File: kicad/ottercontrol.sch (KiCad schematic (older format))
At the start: 75 parts, among them IC1 MAX485, IC2 USBLC6-4, IC3 USBLC6-2SC6, J1 USB_B_Micro, P1 Conn_01x02, Q1 Q_PMOS_GSD, U1 STM32F303CBT6, U2 MAX3051, U6 XL7015, U7 ACT4088, U8 MIC5504-3.3YM5, X1 programmer, X2 Conn_01x08, X3 Conn_01x05, Y1 16MHz

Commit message: placed and routed; preliminary finished
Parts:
- added GND1, VDC1, VDC2: Conn_01x01, TestPoint:TestPoint_THTPad_4.0x4.0mm_Drill2.0mm, symbol Connector_Generic:Conn_01x01
- added R48: 0, Resistor_SMD:R_0603_1608Metric, symbol Device:R
- X1: footprint Connector_PinHeader_2.54mm:PinHeader_2x03_P2.54mm_Vertical -> Connector:Tag-Connect_TC2030-IDC-NL_2x03_P1.27mm_Vertical
- X2: footprint Connector_JST:JST_GH_SM08B-GHS-TB_1x08-1MP_P1.25mm_Horizontal -> Connector_Molex:Molex_PicoBlade_53261-0871_1x08-1MP_P1.25mm_Horizontal
- X3: footprint Connector_JST:JST_GH_SM05B-GHS-TB_1x05-1MP_P1.25mm_Horizontal -> Connector_Molex:Molex_PicoBlade_53261-0571_1x05-1MP_P1.25mm_Horizontal
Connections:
- net RS458_TX is gone; now on net RS485_TX: IC1.4 (DI), U1.21 (PB10)
- net +3V3: now also C5.1, U2.3 (VDD); no longer IC2.5 (VBUS), X3.5 (Pin_5)
- net +5V: now also IC2.5 (VBUS), X3.5 (Pin_5); no longer C5.1, U2.3 (VDD)
- net +VDC: now also VDC1.1 (Pin_1), VDC2.1 (Pin_1)
- net GND: now also R48.2
- net GNDPWR: now also GND1.1 (Pin_1), R48.1
- net at IC3.1 (IO1), J1.2 (D-): now also IC3.6 (IO1), R11.1
- net at IC3.3 (IO2), J1.3 (D+): now also IC3.4 (IO2), R12.2, R14.2
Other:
- moved on the sheet: C24, C25, C26, C27, C28, R11

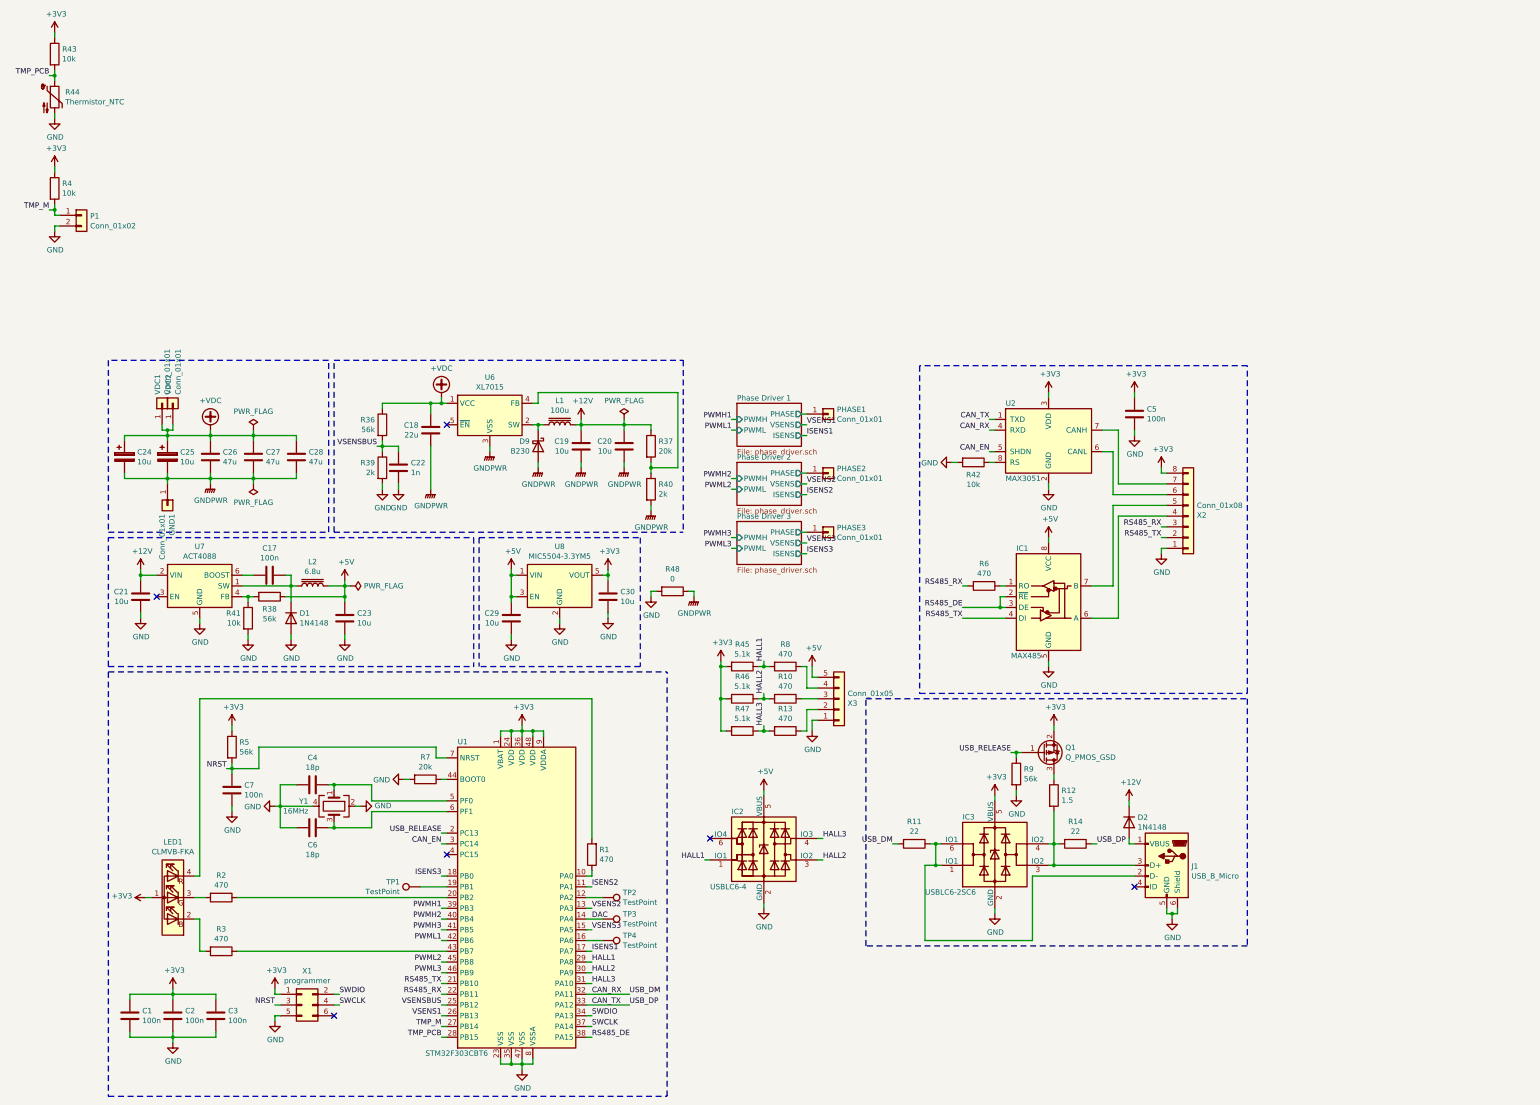
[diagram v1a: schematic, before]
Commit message: made footprint fot mosfets hybrid for TO220 and D2PAK; added jumper instead of 0 Ohm resistor
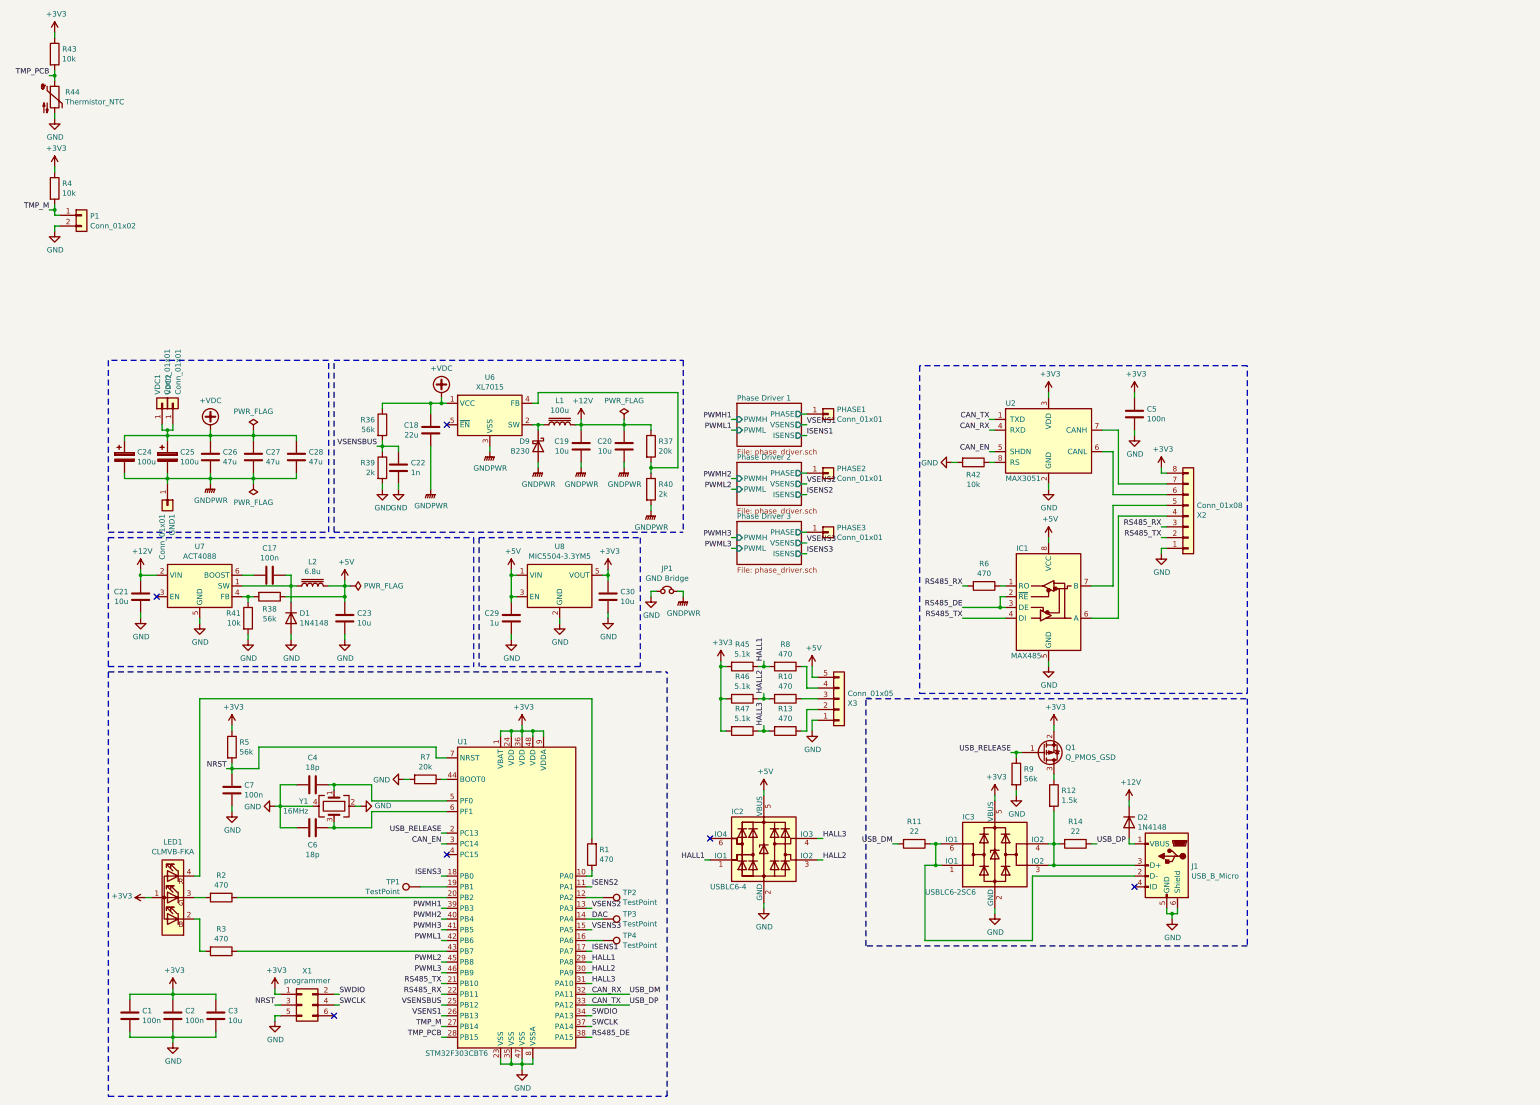
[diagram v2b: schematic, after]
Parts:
- removed R48: 0, Resistor_SMD:R_0603_1608Metric, symbol Device:R
- added JP1: GND Bridge, Jumper:SolderJumper-2_P1.3mm_Bridged_Pad1.0x1.5mm, symbol Device:Jumper_NC_Small
- C1, C2, C5, C7: MPN (none) -> GRM033C81E104KE14E; Voltage Rating DC (none) -> 25
- C17: MPN (none) -> CC0603MRY5V9BB104; Voltage Rating DC (none) -> 50
- C18: MPN (none) -> C5750X7R1E226M250KA; Voltage Rating DC (none) -> 100
- C19, C20, C21: MPN (none) -> TMK316BJ106KL-T; Voltage Rating DC (none) -> 25
- C22: MPN (none) -> 885012206083; Voltage Rating DC (none) -> 50
- C23, C30: MPN (none) -> JMK107ABJ106MA-T; Voltage Rating DC (none) -> 6.3
- C24, C25: value 10u -> 100u; MPN (none) -> 107CKS100MLQ; Voltage Rating DC (none) -> 100
- C26, C27, C28: MPN (none) -> CGA9N3X7R1E476M230KB; Voltage Rating DC (none) -> 100
- C29: value 10u -> 1u; MPN (none) -> 885012106022; Voltage Rating DC (none) -> 10
- C3: value 100n -> 10u; MPN (none) -> JMK107ABJ106MA-T; Voltage Rating DC (none) -> 6.3
- C4, C6: Dielectric (none) -> C0G (NP0); MPN (none) -> GRM0335C1E180FA01D; Tolerance (none) -> 1%
- D1, D2: MPN (none) -> 1N4148WS
- D9: MPN (none) -> B230AE-13
- IC1: MPN (none) -> MAX485CSA+
- IC2: MPN (none) -> USBLC6-4SC6
- IC3: MPN (none) -> USBLC6-2SC6
- L1: MPN (none) -> LPS6235-104MRC
- L2: MPN (none) -> LPS6235-682MRC
- LED1: MPN (none) -> ASMB-MTB0-0A3A2
- R1, R10, R13, R2, R3, R6, R8: MPN (none) -> RC0603FR-07470RL
- R11, R14: MPN (none) -> RC0603FR-0722RL
- R12: value 1.5 -> 1.5k; MPN (none) -> RC0603FR-071K5L
- R36, R38, R5, R9: MPN (none) -> RC0603FR-0756KL
- R37, R7: MPN (none) -> RC0603FR-0720KL
- R39, R40: MPN (none) -> RC0603FR-072KL
- R4, R41, R42, R43: MPN (none) -> RC0603FR-0710KL
- R45, R46, R47: MPN (none) -> RC0603FR-075K1L
- U1: MPN (none) -> STM32F303CBT6
- U2: MPN (none) -> MAX3051ESA+
- U7: MPN (none) -> ACT4088US-T
- U8: MPN (none) -> MIC5504-3.3YM5-TR
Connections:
- net GND: now also JP1.1
- net GNDPWR: now also JP1.2

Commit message: added finished adding MPNs to all components
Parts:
- C29: Voltage Rating DC 10 -> 25
- J1: MPN (none) -> 105017-0001
- JP1, TP1, TP2, TP3, TP4: MPN (none) -> n/a
- P1: renamed from X1; MPN (none) -> TC2030-MCP-NL
- P2: renamed from X2; MPN (none) -> 53261-0871
- P3: renamed from X3; MPN (none) -> 53261-0571
- P4: renamed from P1; MPN (none) -> n/a
- PAD1: renamed from PHASE1; MPN (none) -> n/a
- PAD2: renamed from PHASE2; MPN (none) -> n/a
- PAD3: renamed from PHASE3; MPN (none) -> n/a
- PAD4: renamed from VDC1; MPN (none) -> n/a
- PAD5: renamed from VDC2; MPN (none) -> n/a
- PAD6: renamed from GND1; MPN (none) -> n/a
- Q1: value Q_PMOS_GSD -> Si2367DS; MPN (none) -> SI2367DS-T1-GE3
- R1, R10, R13, R2, R3, R6, R8: MPN RC0603FR-07470RL -> RC0603FR-07100RL
- Y1: footprint Crystal:Crystal_SMD_5032-4Pin_5.0x3.2mm -> Crystal:Crystal_SMD_3225-4Pin_3.2x2.5mm; MPN (none) -> FA-238 16.0000MB-K3
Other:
- moved on the sheet: C29, C30, C5, D2, IC1, IC2, IC3, J1, JP1, P2, P3, P4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

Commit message: finalyzed design
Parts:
- removed IC3: USBLC6-2SC6, Package_TO_SOT_SMD:SOT-23-6, symbol Power_Protection:USBLC6-2SC6
- removed LED1: CLMVB-FKA, LED_SMD:LED_Cree-PLCC4_2x2mm_CW, symbol LED:ASMB-MTB0-0A3A2
- added IC3: USBLC6-4, Package_TO_SOT_SMD:SOT-23-6, symbol Power_Protection:USBLC6-4
- added LED1: LED_RABG, LED_SMD:LED_Avago_PLCC4_3.2x2.8mm_CW, symbol Device:LED_RABG
- C19, C20, C21: Aliexpress (none) -> https://www.aliexpress.com/item//32880416347.html
- C24, C25: Aliexpress (none) -> https://www.aliexpress.com/item//32642894401.html
- C26, C27, C28: Aliexpress (none) -> https://www.aliexpress.com/item//32826554052.html
- D9: Aliexpress (none) -> https://www.aliexpress.com/item//32855500127.html
- IC1: Aliexpress (none) -> https://de.aliexpress.com/item//32876836472.html
- IC2: Aliexpress (none) -> https://www.aliexpress.com/item//32917098748.html
- J1: Aliexpress (none) -> https://www.aliexpress.com/item//32857135081.html
- L1, L2: Aliexpress (none) -> https://de.aliexpress.com/item//32886534770.html
- P2: Aliexpress (none) -> https://de.aliexpress.com/item//32799039952.html
- P3: Aliexpress (none) -> https://de.aliexpress.com/item//32798651089.html
- Q1: Aliexpress (none) -> https://de.aliexpress.com/item//32964492474.html
- U1: Aliexpress (none) -> https://www.aliexpress.com/item//32745913400.html
- U2: Aliexpress (none) -> https://www.aliexpress.com/item//32915140112.html
- U6: Aliexpress (none) -> https://de.aliexpress.com/item//32955190374.html; MPN (none) -> XL7015
- U7: Aliexpress (none) -> https://de.aliexpress.com/item//32251221271.html
- U8: Aliexpress (none) -> https://de.aliexpress.com/item//32271737578.html
- Y1: Aliexpress (none) -> https://www.aliexpress.com/item//32851252873.html
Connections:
- net +3V3: now also IC3.5 (VBUS), LED1.2 (A)
- net GND: now also IC3.2 (GND)
- net at J1.2 (D-), R11.1: now also IC3.1 (IO1), IC3.6 (IO4)
- net at J1.3 (D+), R12.2, R14.2: now also IC3.3 (IO2), IC3.4 (IO3)
- net at R3.2: now also LED1.3 (BK)
- net at R2.2: now also LED1.4 (GK)
- net at R1.2: now also LED1.1 (RK)
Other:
- note added: "Cable Connector: 51021-0500\nhttps://de.aliexpress.com/item//32819174211.html"
- note added: "Cable Connector: 51021-0800\nhttps://de.aliexpress.com/item//32310864974.html"
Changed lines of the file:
@@
 encoding utf-8
 Sheet 1 4
-Title ""
-Date ""
+Title "ottercontrol"
+Date "2019-01-07"
 Rev ""
 Comp ""
@@
 F 3 "https://www.mouser.de/datasheet/2/389/stm32f303cb-956188.pdf" H 4350 5500 50  0001 C CNN
 F 4 "STM32F303CBT6" H 0   0   50  0001 C CNN "MPN"
+F 5 "https://www.aliexpress.com/item//32745913400.html" H 4350 5500 50  0001 C CNN "Aliexpress"
 	1    4350 5500
 	1    0    0    -1
@@
 F 3 "https://www.mouser.de/datasheet/2/137/A-238_en-932914.pdf" H 2600 4650 50  0001 C CNN
 F 4 "FA-238 16.0000MB-K3" H 0   0   50  0001 C CNN "MPN"
+F 5 "https://www.aliexpress.com/item//32851252873.html" V 2600 4650 50  0001 C CNN "Aliexpress"
 	1    2600 4650
 	0    1    1    0
@@
 F 3 "https://www.mouser.de/datasheet/2/256/MAX3051-1280983.pdf" H 9300 3550 50  0001 C CNN
 F 4 "MAX3051ESA+" H 50  2300 50  0001 C CNN "MPN"
+F 5 "https://www.aliexpress.com/item//32915140112.html" H 9300 3550 50  0001 C CNN "Aliexpress"
 	1    9300 3550
 	1    0    0    -1
@@
 F 3 "https://www.mouser.de/datasheet/2/256/MAX490-1389177.pdf" H 9300 5050 50  0001 C CNN
 F 4 "MAX485CSA+" H 50  2300 50  0001 C CNN "MPN"
+F 5 "https://de.aliexpress.com/item//32876836472.html" H 9300 5000 50  0001 C CNN "Aliexpress"
 	1    9300 5000
 	1    0    0    -1
@@
 F 3 "https://www.mouser.de/datasheet/2/276/0532610871_PCB_HEADERS-171054.pdf" H 10600 4250 50  0001 C CNN
 F 4 "53261-0871" H 50  2300 50  0001 C CNN "MPN"
+F 5 "https://de.aliexpress.com/item//32799039952.html" H 10600 4250 50  0001 C CNN "Aliexpress"
 	1    10600 4250
 	1    0    0    1
@@
 F 3 "https://www.mouser.de/datasheet/2/276/1050170001_IO_CONNECTORS-230168.pdf" H 10550 2000 50  0001 C CNN
 F 4 "105017-0001" H 50  -3150 50  0001 C CNN "MPN"
+F 5 "https://www.aliexpress.com/item//32857135081.html" H 10400 2050 50  0001 C CNN "Aliexpress"
 	1    10400 2050
 	-1   0    0    -1
@@
 F 3 "" H 8800 2500 50  0001 C CNN
 	1    8800 2500
-	1    0    0    -1
-$EndComp
-$Comp
-L Power_Protection:USBLC6-2SC6 IC3
-U 1 1 5C2EDA2E
-P 8800 1950
-F 0 "IC3" H 8500 2300 50  0000 L CNN
-F 1 "USBLC6-2SC6" H 8150 1600 50  0000 L CNN
-F 2 "Package_TO_SOT_SMD:SOT-23-6" H 8050 2350 50  0001 C CNN
-F 3 "https://www.mouser.de/datasheet/2/389/usblc6-2-957370.pdf" H 9000 2300 50  0001 C CNN
-F 4 "USBLC6-2SC6" H 50  -3150 50  0001 C CNN "MPN"
-	1    8800 1950
 	1    0    0    -1
 $EndComp
@@
 F 3 "https://www.mouser.de/datasheet/2/427/si2367ds-278436.pdf" H 9250 1000 50  0001 C CNN
 F 4 "SI2367DS-T1-GE3" H 50  -3150 50  0001 C CNN "MPN"
+F 5 "https://de.aliexpress.com/item//32964492474.html" H 9250 1000 50  0001 C CNN "Aliexpress"
 	1    9250 1000
 	1    0    0    1
@@
 $EndComp
 $Comp
-L LED:ASMB-MTB0-0A3A2 LED1
-U 1 1 5C47CE93
-P 1100 5500
-F 0 "LED1" H 1100 6017 50  0000 C CNN
-F 1 "CLMVB-FKA" H 1100 5926 50  0000 C CNN
-F 2 "LED_SMD:LED_Cree-PLCC4_2x2mm_CW" H 1100 6000 50  0001 C CNN
-F 3 "https://www.mouser.de/datasheet/2/678/V02-4186EN_DS_ASMB-MTB0_2014-09-10-909697.pdf" H 1100 5050 50  0001 C CNN
-F 4 "ASMB-MTB0-0A3A2" H 0   0   50  0001 C CNN "MPN"
-	1    1100 5500
-	-1   0    0    -1
-$EndComp
-$Comp
 L Regulator_Switching:APE1707H-12-HF U6
 U 1 1 5C58F2E9
@@
 F 2 "Package_TO_SOT_SMD:TO-252-5_TabPin3" H 4075 750 50  0001 L CIN
 F 3 "http://pdf.datasheet.live/datasheets-1/advanced_power_electronics/APE1707H-12-HF.pdf" H 4050 1000 50  0001 C CNN
-F 4 "" H 0   0   50  0001 C CNN "MPN"
+F 4 "XL7015" H 4150 1442 50  0001 C CNN "MPN"
+F 5 "https://de.aliexpress.com/item//32955190374.html" H 4050 1000 50  0001 C CNN "Aliexpress"
 	1    4050 1000
 	1    0    0    -1
@@
 F 3 "https://www.mouser.de/datasheet/2/115/B220AEBE-B245AEBE-1115122.pdf" H 4500 1300 50  0001 C CNN
 F 4 "B230AE-13" H 0   0   50  0001 C CNN "MPN"
+F 5 "https://www.aliexpress.com/item//32855500127.html" V 4500 1300 50  0001 C CNN "Aliexpress"
 	1    4500 1300
 	0    1    1    0
@@
 F 4 "25" H 4900 1300 50  0001 C CNN "Voltage Rating DC"
 F 5 "TMK316BJ106KL-T" H 0   0   50  0001 C CNN "MPN"
+F 6 "https://www.aliexpress.com/item//32880416347.html" H 4900 1300 50  0001 C CNN "Aliexpress"
 	1    4900 1300
 	1    0    0    -1
@@
 F 4 "25" H 5300 1300 50  0001 C CNN "Voltage Rating DC"
 F 5 "TMK316BJ106KL-T" H 0   0   50  0001 C CNN "MPN"
+F 6 "https://www.aliexpress.com/item//32880416347.html" H 5300 1300 50  0001 C CNN "Aliexpress"
 	1    5300 1300
 	1    0    0    -1
@@
 F 3 "https://www.mouser.de/datasheet/2/631/ACT4088_Datasheet-1291541.pdf" H 1250 2700 50  0001 C CNN
 F 4 "ACT4088US-T" H 0   0   50  0001 C CNN "MPN"
+F 5 "https://de.aliexpress.com/item//32251221271.html" H 1350 2600 50  0001 C CNN "Aliexpress"
 	1    1350 2600
 	1    0    0    -1
@@
 F 4 "25" H 800 2700 50  0001 C CNN "Voltage Rating DC"
 F 5 "TMK316BJ106KL-T" H 0   0   50  0001 C CNN "MPN"
+F 6 "https://www.aliexpress.com/item//32880416347.html" H 800 2700 50  0001 C CNN "Aliexpress"
 	1    800  2700
 	1    0    0    -1
@@
 F 3 "https://www.mouser.de/datasheet/2/597/lps6235-270704.pdf" H 2400 2600 50  0001 C CNN
 F 4 "LPS6235-682MRC" H 0   0   50  0001 C CNN "MPN"
+F 5 "https://de.aliexpress.com/item//32886534770.html" V 2400 2600 50  0001 C CNN "Aliexpress"
 	1    2400 2600
 	0    -1   -1   0
@@
 F 3 "https://www.mouser.de/datasheet/2/597/lps6235-270704.pdf" H 4700 1100 50  0001 C CNN
 F 4 "LPS6235-104MRC" H 0   0   50  0001 C CNN "MPN"
+F 5 "https://de.aliexpress.com/item//32886534770.html" V 4700 1100 50  0001 C CNN "Aliexpress"
 	1    4700 1100
 	0    -1   -1   0
@@
 F 3 "https://www.mouser.de/datasheet/2/268/MIC550X-1082389.pdf" H 4200 2850 50  0001 C CNN
 F 4 "MIC5504-3.3YM5-TR" H -250 0   50  0001 C CNN "MPN"
+F 5 "https://de.aliexpress.com/item//32271737578.html" H 4450 2600 50  0001 C CNN "Aliexpress"
 	1    4450 2600
 	1    0    0    -1
@@
 F 4 "100" H 868 1546 50  0001 C CNN "Voltage Rating DC"
 F 5 "107CKS100MLQ" H 0   0   50  0001 C CNN "MPN"
+F 6 "https://www.aliexpress.com/item//32642894401.html" H 650 1400 50  0001 C CNN "Aliexpress"
 	1    650  1400
 	1    0    0    -1
@@
 F 4 "100" H 1268 1546 50  0001 C CNN "Voltage Rating DC"
 F 5 "107CKS100MLQ" H 0   0   50  0001 C CNN "MPN"
+F 6 "https://www.aliexpress.com/item//32642894401.html" H 1050 1400 50  0001 C CNN "Aliexpress"
 	1    1050 1400
 	1    0    0    -1
@@
 F 4 "100" H 1450 1400 50  0001 C CNN "Voltage Rating DC"
 F 5 "CGA9N3X7R1E476M230KB" H 0   0   50  0001 C CNN "MPN"
+F 6 "https://www.aliexpress.com/item//32826554052.html" H 1450 1400 50  0001 C CNN "Aliexpress"
 	1    1450 1400
 	1    0    0    -1
@@
 F 4 "100" H 1850 1400 50  0001 C CNN "Voltage Rating DC"
 F 5 "CGA9N3X7R1E476M230KB" H 0   0   50  0001 C CNN "MPN"
+F 6 "https://www.aliexpress.com/item//32826554052.html" H 1850 1400 50  0001 C CNN "Aliexpress"
 	1    1850 1400
 	1    0    0    -1
@@
 F 4 "100" H 2465 1546 50  0001 C CNN "Voltage Rating DC"
 F 5 "CGA9N3X7R1E476M230KB" H 0   0   50  0001 C CNN "MPN"
+F 6 "https://www.aliexpress.com/item//32826554052.html" H 2250 1400 50  0001 C CNN "Aliexpress"
 	1    2250 1400
 	1    0    0    -1
@@
 F 3 "https://www.mouser.de/datasheet/2/276/0532610571_PCB_HEADERS-170968.pdf" H 7150 1100 50  0001 C CNN
 F 4 "53261-0571" H -150 -2550 50  0001 C CNN "MPN"
+F 5 "https://de.aliexpress.com/item//32798651089.html" H 7150 1100 50  0001 C CNN "Aliexpress"
 	1    7150 1100
 	1    0    0    1
@@
 F 3 "https://www.mouser.de/datasheet/2/389/usblc6-4-957459.pdf" H 6750 2650 50  0001 C CNN
 F 4 "USBLC6-4SC6" H -50 -2750 50  0001 C CNN "MPN"
+F 5 "https://de.aliexpress.com/item//32916288820.html" H 6550 2300 50  0001 C CNN "Aliexpress"
+F 6 "https://www.aliexpress.com/item//32917098748.html" H 6550 2300 50  0001 C CNN "Aliexpress"
 	1    6550 2300
 	1    0    0    -1
@@
 Wire Notes Line
 	5900 5150 7800 5150
+Text Notes 5900 350  0    50   ~ 0
+Cable Connector: 51021-0500\nhttps://de.aliexpress.com/item//32819174211.html
+Text Notes 11350 4300 0    50   ~ 0
+Cable Connector: 51021-0800\nhttps://de.aliexpress.com/item//32310864974.html
+$Comp
+L Power_Protection:USBLC6-4 IC3
+U 1 1 5C3D8F60
+P 8800 1950
+F 0 "IC3" H 8500 2300 50  0000 L CNN
+F 1 "USBLC6-4" H 8300 1600 50  0000 L CNN
+F 2 "Package_TO_SOT_SMD:SOT-23-6" H 8050 2350 50  0001 C CNN
+F 3 "https://www.mouser.de/datasheet/2/389/usblc6-4-957459.pdf" H 9000 2300 50  0001 C CNN
+F 4 "USBLC6-4SC6" H 2200 -3100 50  0001 C CNN "MPN"
+F 5 "https://de.aliexpress.com/item//32916288820.html" H 8800 1950 50  0001 C CNN "Aliexpress"
+F 6 "https://www.aliexpress.com/item//32917098748.html" H 8800 1950 50  0001 C CNN "Aliexpress"
+	1    8800 1950
+	1    0    0    -1
+$EndComp
+$Comp
+L Device:LED_RABG LED1
+U 1 1 5C40BD05
+P 1100 5500
+F 0 "LED1" H 1100 5997 50  0000 C CNN
+F 1 "LED_RABG" H 1100 5906 50  0000 C CNN
+F 2 "LED_SMD:LED_Avago_PLCC4_3.2x2.8mm_CW" H 1100 5450 50  0001 C CNN
+F 3 "~" H 1100 5450 50  0001 C CNN
+F 4 "https://www.aliexpress.com/item//32493858500.html" H 1100 5500 50  0001 C CNN "Aliexpress"
+	1    1100 5500
+	-1   0    0    -1
+$EndComp
 $EndSCHEMATC
